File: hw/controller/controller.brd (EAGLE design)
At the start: 46 x 53 mm, 97 parts, among them IC1 STM32G474CEU6, J1 XT30XT30PW_MALE, J2 XT30XT30PW_MALE, Q1 TPH1R204PLSOP_ADVANCE_8, Q2 TPH1R204PLSOP_ADVANCE_8, Q3 TPH1R204PLSOP_ADVANCE_8, Q4 TPH1R204PLSOP_ADVANCE_8, Q5 TPH1R204PLSOP_ADVANCE_8, Q6 TPH1R204PLSOP_ADVANCE_8, U2 DRV8323RS, U3 AS5147, U4 TCAN334G

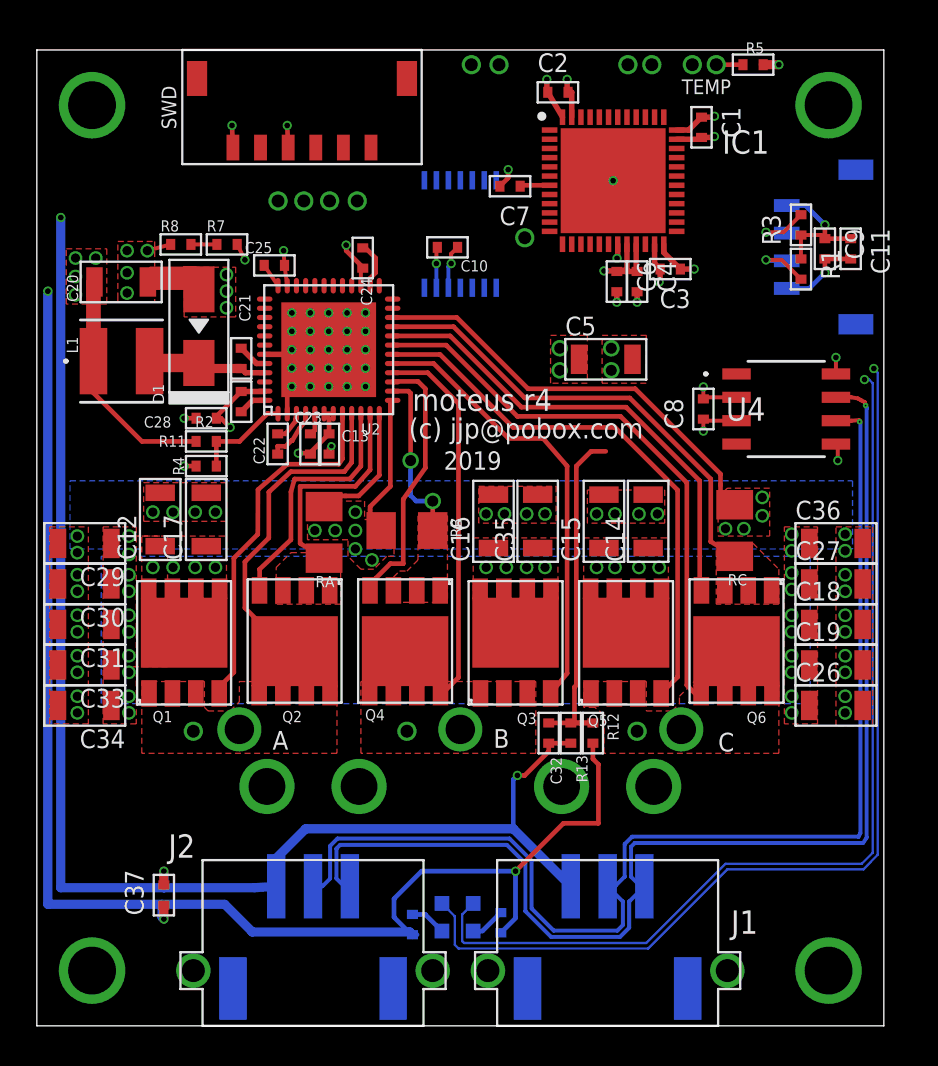
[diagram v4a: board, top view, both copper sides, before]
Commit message: All silks rough placed and all part numbers fixed up
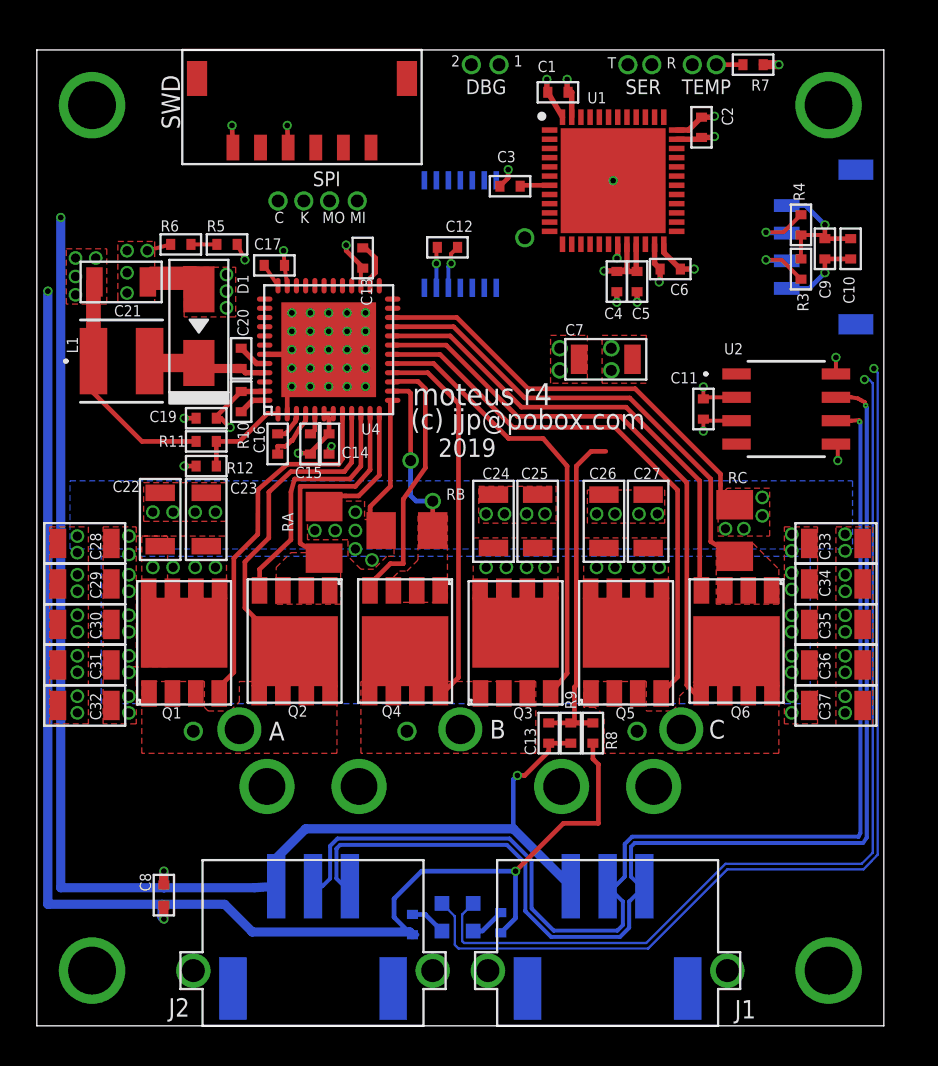
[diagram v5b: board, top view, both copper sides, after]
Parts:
- removed R13: 10k 1%, mfpassives:R0402
- added R10: 100k 1%, mfpassives:R0402
- C1, C10, C11, C13, C2, C3, C8: value 0.1uF 50V -> 0.1uF
- C12, C18, C5: value 10uF -> 0.1uF; device mfpassives:C1206 -> mfpassives:C0402
- C14, C16, C20: value 10uF -> 0.1uF 50V; device mfpassives:C1206 -> mfpassives:C0402
- C15, C17: value 10uF -> 1uF; device mfpassives:C1206 -> mfpassives:C0402
- C19: value 10uF -> 0.47uF 50V; device mfpassives:C1206 -> mfpassives:C0402
- C21, C22, C32, C37, C7: value 0.1uF 50V -> 10uF; device mfpassives:C0402 -> mfpassives:C1206
- C23, C24, C25, C28: value 1.5uF 35V -> 10uF; device mfpassives:C0402 -> mfpassives:C1206
- C4: value 0.1uF 50V -> 1uF
- C6: value 1uF -> 0.1uF
- R1: value 2k -> 220
- R12: value 47k NTC -> 10k 1%
- R2: value 100k 1% -> 220
- R4: value 10k 1% -> 2k
- R5: value 10k 1% -> 100k 1%
- R6, R9: value 220 -> 10k 1%
- R7: value 100k 1% -> 10k 1%
- R8: value 10k 1% -> 47k NTC
- U2: value DRV8323RS -> TCAN334G; device controller:PVQFN-N48 -> controller:SOT23-8
- U4: value TCAN334G -> DRV8323RS; device controller:SOT23-8 -> controller:PVQFN-N48
- moved R1 41.4 mm to (-2.60, -37.5), flipped to the bottom, turned to 90 degrees
- moved C33 41.3 mm to (20.4, -16.8), turned to 0 degrees
- moved C34 41.3 mm to (20.4, -19.0), turned to 0 degrees
- moved C8 39.4 mm to (-16.1, -35.9)
- moved R6 39.0 mm to (-15.2, -0.56), flipped to the top, turned to 0 degrees
- moved C37 37.9 mm to (20.4, -25.6), turned to 0 degrees
- moved C19 36.7 mm to (-13.8, -10.0), turned to 180 degrees
- moved R4 34.9 mm to (18.5, 0.50), turned to 90 degrees
- moved R8 34.7 mm to (7.20, -27.1), turned to 90 degrees
- moved C18 32.5 mm to (-5.30, -1.30), turned to 90 degrees
- moved R2 31.6 mm to (2.20, -37.4), flipped to the bottom
- moved R5 30.2 mm to (-12.7, -0.56)
- moved R7 30.2 mm to (15.9, 9.20)
- moved R12 25.5 mm to (-13.8, -12.6), turned to 180 degrees
- moved C32 25.2 mm to (-20.4, -25.6), turned to 180 degrees
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- renumbered IC1 to U1, U$12 to M2, U$13 to M3, U$14 to M4, U$9 to M1
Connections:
- net +3V3: now also C12.P$1, C18.P$2, C21.P$1, C5.P$1, C7.P$2, R2.P$1, R4.P$1, R8.P$1, U2.3, U4.26; no longer C20.P$1, C24.P$2, C3.P$1, C37.P$1, C5.P$2, R12.P$1, R6.P$1, R9.P$1, U2.26, U4.3
- net CAN_N: now also U2.6; no longer U4.6
- net CAN_P: now also U2.7; no longer U4.7
- net CAN_RX: now also U2.4; no longer U4.4
- net CAN_TX: now also U2.1; no longer U4.1
- net CUR1: now also U4.25; no longer U2.25
- net CUR2: now also U4.24; no longer U2.24
- net CUR3: now also U4.23; no longer U2.23
- net DRV8323_CS: now also U4.32; no longer U2.32
- net DRV8323_MISO: now also U4.29; no longer U2.29
- net DRV8323_MOSI: now also U4.30; no longer U2.30
- net DRV8323_SCLK: now also U4.31; no longer U2.31
- net GHA: now also U4.8; no longer U2.8
- net GHB: now also U4.17; no longer U2.17
- net GHC: now also U4.18; no longer U2.18
- net GLA: now also U4.10; no longer U2.10
- net GLB: now also U4.15; no longer U2.15
- net GLC: now also U4.20; no longer U2.20
- net GND: now also C12.P$2, C13.P$2, C17.P$1, C18.P$1, C21.P$2, C5.P$2, C7.P$1, R6.P$1, R7.P$2, R9.P$2, U2.2, U2.5, U2.8, U4.27, U4.35; no longer C20.P$2, C24.P$1, C25.P$1, C32.P$2, C37.P$2, C5.P$1, C7.P$2, R13.P$2, R5.P$2, R8.P$1, U2.27, U2.35, U4.2, U4.5, U4.8
- net I2C_ABS_SCL: now also R4.P$2; no longer R3.P$2
- net I2C_ABS_SDA: now also R3.P$2; no longer R1.P$2
- net MOTOR1: now also U4.37; no longer U2.37
- net MOTOR2: now also U4.39; no longer U2.39
- net MOTOR3: now also U4.41; no longer U2.41
- net MOTOR_ENABLE: now also U4.33; no longer U2.33
- net MOTOR_FAULT: now also U4.28; no longer U2.28
- net MOTOR_HIZ: now also U4.38, U4.40, U4.42; no longer U2.38, U2.40, U2.42
- net N$10: now also C16.P$2, U4.3; no longer C22.P$2, U2.3
- net N$11: now also C20.P$2, U4.45; no longer C21.P$2, U2.45
- net N$12: now also C20.P$1, U4.44; no longer C21.P$1, U2.44
- net N$13: now also C16.P$1, U4.4; no longer C22.P$1, U2.4
- net N$14: now also C15.P$2, U4.5; no longer C23.P$2, U2.5
- net N$16: now also C17.P$2, U4.36; no longer C25.P$2, U2.36
- net N$17: now also R1.P$2; no longer R6.P$2
- net N$18: now also R2.P$2; no longer R9.P$2
- net N$5: now also R10.P$1, U4.48; no longer R2.P$1, U2.48
- net N$8: now also R12.P$1, U4.1; no longer R4.P$1, U2.1
- net NRST: now also C3.P$1; no longer C7.P$1
- net SHA: now also U4.9; no longer U2.9
- net SHB: now also U4.16; no longer U2.16
- net SHC: now also U4.19; no longer U2.19
- net SNA: now also U4.12; no longer U2.12
- net SNB: now also U4.13; no longer U2.13
- net SNC: now also U4.22; no longer U2.22
- net SPA: now also U4.11; no longer U2.11
- net SPB: now also U4.14; no longer U2.14
- net SPC: now also U4.21; no longer U2.21
- net V+: now also C22.P$1, C24.P$1, C25.P$1, C32.P$1, C37.P$1, R10.P$2, R5.P$2, U4.47, U4.6, U4.7; no longer C12.P$1, C13.P$1, C16.P$1, C17.P$1, C18.P$1, R2.P$2, R7.P$2, U2.47, U2.6, U2.7
- net V-: now also C22.P$2, C23.P$2, C24.P$2, C25.P$2, C32.P$2, C37.P$2, R12.P$2, U4.2, U4.43, U4.P1, U4.P10, U4.P11, U4.P12, U4.P13, U4.P14, U4.P15, U4.P16, U4.P17, U4.P18, U4.P19, U4.P2, U4.P20, U4.P21, U4.P22, U4.P23, U4.P24, U4.P25, U4.P3, U4.P4, U4.P5, U4.P6, U4.P7, U4.P8, U4.P9, U4.PAD; no longer C12.P$2, C13.P$2, C15.P$2, C16.P$2, C17.P$2, C18.P$2, R4.P$2, U2.2, U2.43, U2.P1, U2.P10, U2.P11, U2.P12, U2.P13, U2.P14, U2.P15, U2.P16, U2.P17, U2.P18, U2.P19, U2.P2, U2.P20, U2.P21, U2.P22, U2.P23, U2.P24, U2.P25, U2.P3, U2.P4, U2.P5, U2.P6, U2.P7, U2.P8, U2.P9, U2.PAD
- net VBAT_SENSE: now also R5.P$1, R6.P$2; no longer R7.P$1, R8.P$2
- net VTEMP_FET: now also C13.P$1, R8.P$2, R9.P$1; no longer C32.P$1, R12.P$2, R13.P$1
- net VTEMP_MOT: now also R7.P$1; no longer R5.P$1
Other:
- board text added: "1"
- board text added: "2"
- board text added: "DBG"
- board text added: "K"
- board text added: "MI"
- board text added: "MO"
- board text added: "R"
- board text added: "SER"
- board text added: "SPI"
- board text added: "T"

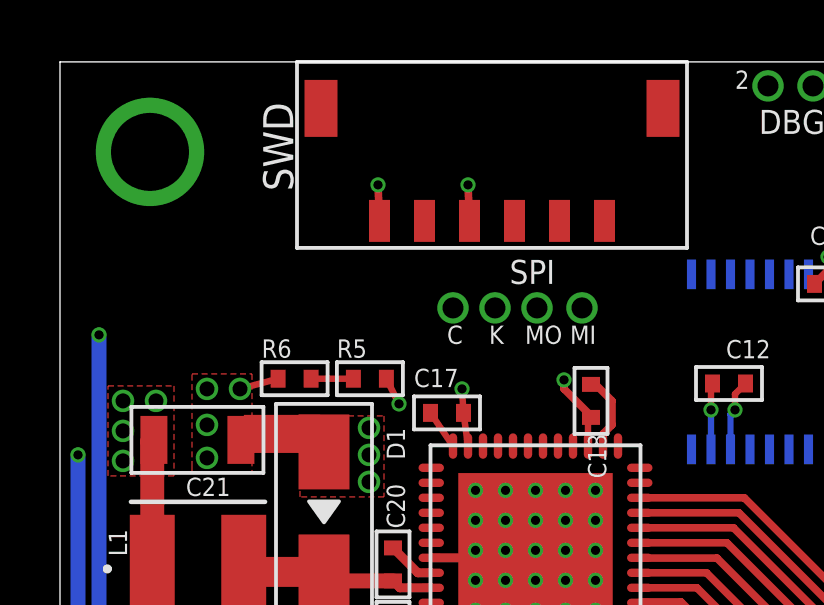
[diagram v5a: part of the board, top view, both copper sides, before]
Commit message: Added some more debugging pads
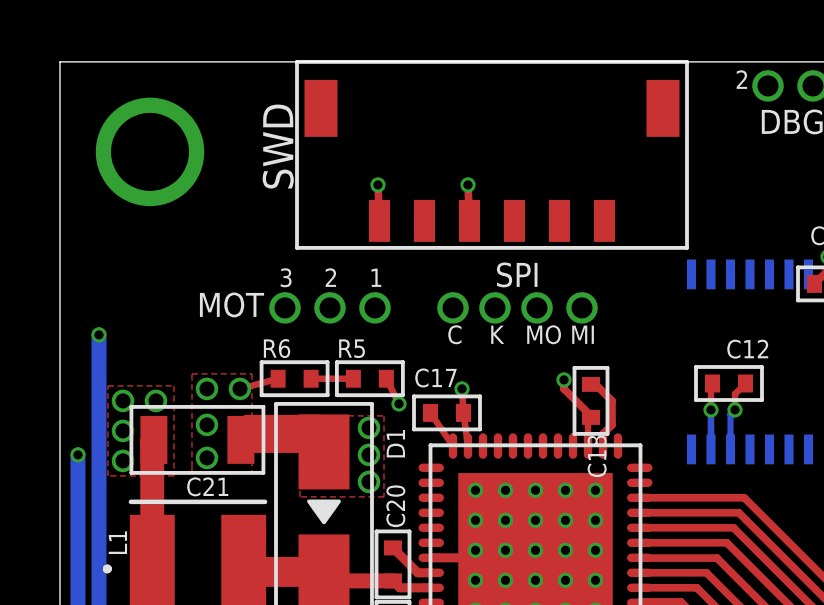
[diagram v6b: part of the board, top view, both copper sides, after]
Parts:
- added MOT1, MOT2, MOT3: PAD24AWG_PAD, controller:24AWG_PAD
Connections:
- net MOTOR1: now also MOT1.P$1
- net MOTOR2: now also MOT2.P$1
- net MOTOR3: now also MOT3.P$1
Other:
- board text added: "3"
- board text added: "MOT"
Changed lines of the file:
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@@
 <layers>
 <layer number="1" name="Top" color="4" fill="1" visible="yes" active="yes"/>
-<layer number="2" name="Route2" color="1" fill="3" visible="no" active="yes"/>
+<layer number="2" name="Route2" color="1" fill="3" visible="yes" active="yes"/>
 <layer number="3" name="Route3" color="4" fill="3" visible="no" active="no"/>
 <layer number="4" name="Route4" color="1" fill="4" visible="no" active="no"/>
@@
 <layer number="13" name="Route13" color="4" fill="5" visible="no" active="no"/>
 <layer number="14" name="Route14" color="1" fill="6" visible="no" active="no"/>
-<layer number="15" name="Route15" color="4" fill="6" visible="no" active="yes"/>
+<layer number="15" name="Route15" color="4" fill="6" visible="yes" active="yes"/>
 <layer number="16" name="Bottom" color="1" fill="1" visible="yes" active="yes"/>
 <layer number="17" name="Pads" color="2" fill="1" visible="yes" active="yes"/>
@@
 <text x="-0.5" y="9.1" size="0.6096" layer="21" font="vector">2</text>
 <text x="2.9" y="9.1" size="0.6096" layer="21" font="vector">1</text>
-<text x="-6.5" y="3.4" size="0.8" layer="21" rot="R180">SPI</text>
+<text x="-8.5" y="2.5" size="0.8" layer="21">SPI</text>
 <text x="-10.1" y="0.6" size="0.6096" layer="21" font="vector">C</text>
 <text x="-8.7" y="0.6" size="0.6096" layer="21" font="vector">K</text>
 <text x="-7.5" y="0.6" size="0.6096" layer="21" font="vector">MO</text>
 <text x="-6" y="0.6" size="0.6096" layer="21" font="vector">MI</text>
+<text x="-12.7" y="2.5" size="0.6096" layer="21" font="vector">1</text>
+<text x="-14.2" y="2.5" size="0.6096" layer="21" font="vector">2</text>
+<text x="-15.7" y="2.5" size="0.6096" layer="21" font="vector">3</text>
+<text x="-16.2" y="2.3" size="0.8" layer="21" rot="R180">MOT</text>
 </plain>
 <attributes>
@@
 <attribute name="POPULATE" value="0" x="-8.5" y="1.8" size="1.778" layer="27" display="off"/>
 </element>
+<element name="MOT1" library="controller" package="24AWG_PAD" value="PAD24AWG_PAD" x="-12.5" y="1.8">
+<attribute name="POPULATE" value="0" x="-12.5" y="1.8" size="0.6096" layer="27" font="vector" display="off"/>
+</element>
+<element name="MOT2" library="controller" package="24AWG_PAD" value="PAD24AWG_PAD" x="-14" y="1.8">
+<attribute name="POPULATE" value="0" x="-14" y="1.8" size="0.6096" layer="27" font="vector" display="off"/>
+</element>
+<element name="MOT3" library="controller" package="24AWG_PAD" value="PAD24AWG_PAD" x="-15.5" y="1.8">
+<attribute name="POPULATE" value="0" x="-15.5" y="1.8" size="0.6096" layer="27" font="vector" display="off"/>
+</element>
 </elements>
 <signals>
@@
 <contactref element="U4" pad="37"/>
 <contactref element="U1" pad="8"/>
+<contactref element="MOT1" pad="P$1"/>
+<wire x1="-10.625" y1="-3.53" x2="-12.5" y2="1.8" width="0" layer="19" extent="1-1"/>
 <wire x1="4.85" y1="2.15" x2="-10.625" y2="-3.53" width="0" layer="19" extent="1-1"/>
 </signal>
@@
 <contactref element="U4" pad="39"/>
 <contactref element="U1" pad="9"/>
+<contactref element="MOT2" pad="P$1"/>
+<wire x1="-14" y1="1.8" x2="-10.625" y2="-4.53" width="0" layer="19" extent="1-1"/>
 <wire x1="4.85" y1="1.65" x2="-10.625" y2="-4.53" width="0" layer="19" extent="1-1"/>
 </signal>
@@
 <contactref element="U4" pad="41"/>
 <contactref element="U1" pad="10"/>
+<contactref element="MOT3" pad="P$1"/>
+<wire x1="-15.5" y1="1.8" x2="-10.625" y2="-5.53" width="0" layer="19" extent="1-1"/>
 <wire x1="4.85" y1="1.15" x2="-10.625" y2="-5.53" width="0" layer="19" extent="1-1"/>
 </signal>

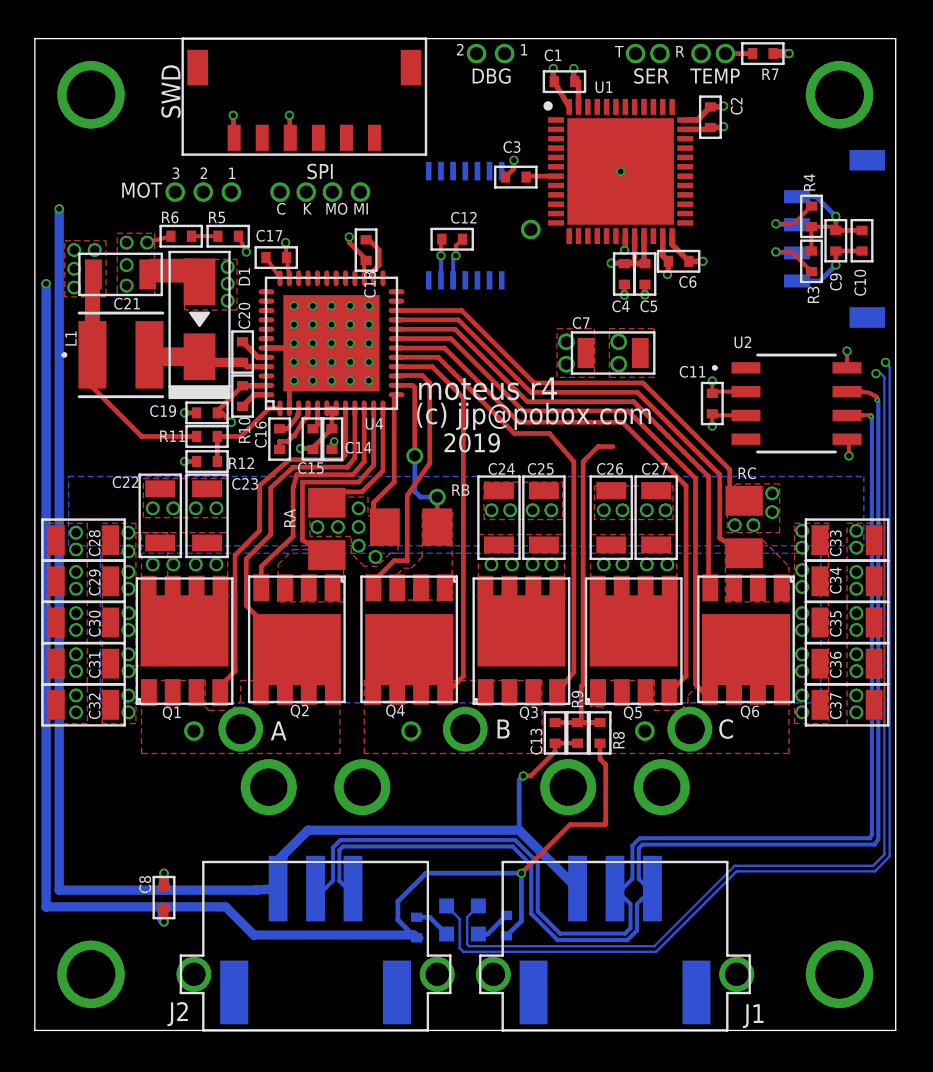
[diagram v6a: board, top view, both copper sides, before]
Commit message: Nearly final version
Still need to verify the footprints of all the JST connectors
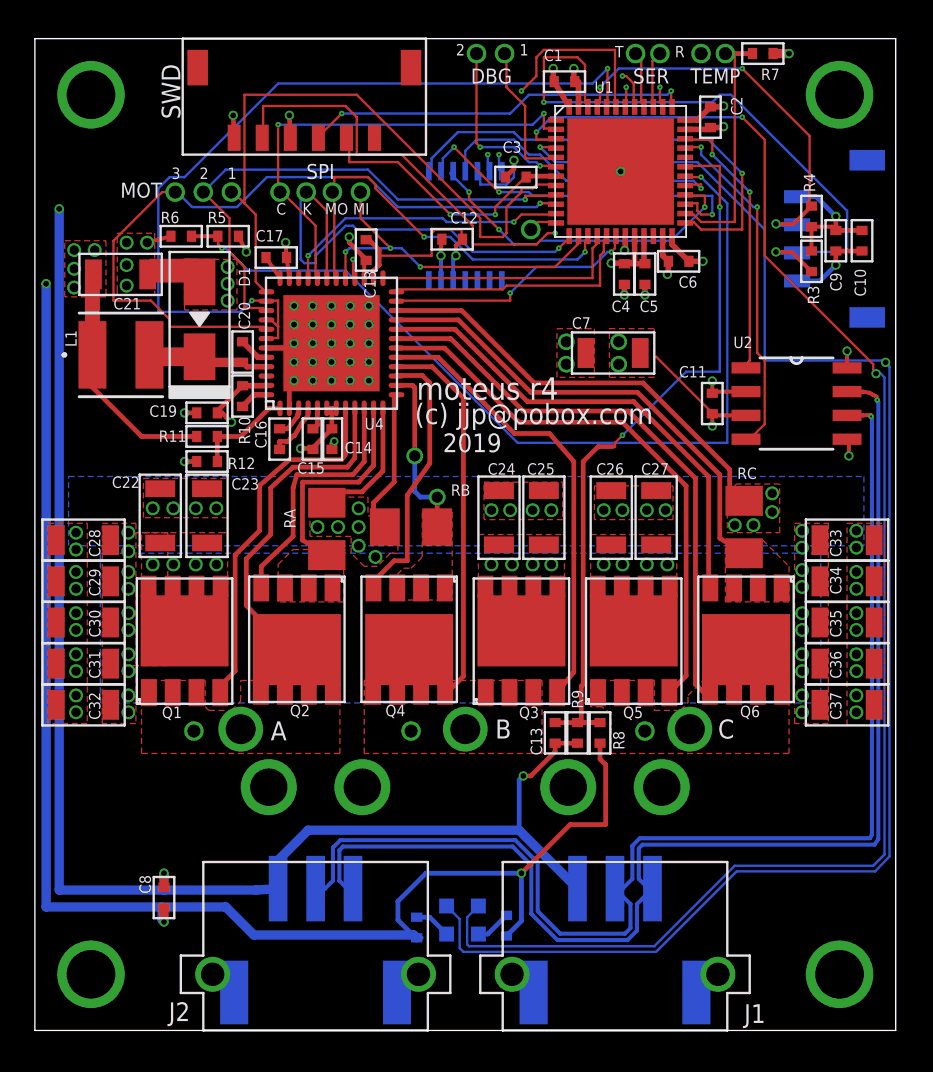
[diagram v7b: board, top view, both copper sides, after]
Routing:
- net VBAT_SENSE: track 1.41 -> 49.1 mm, vias 0 -> 2
- net MOTOR_HIZ: track 0.00 -> 45.4 mm, vias 0 -> 2
- net MOTOR3: track 0.00 -> 38.7 mm, vias 0 -> 1
- net MOTOR1: track 0.00 -> 34.5 mm
- net SWCLK: track 0.00 -> 33.7 mm, vias 0 -> 2
- net I2C_ABS_SDA: track 3.49 -> 34.4 mm, vias 1 -> 2
- net LED2: track 52.8 -> 82.3 mm, vias 1 -> 3
- net MOTOR2: track 0.00 -> 28.6 mm, vias 0 -> 1
- net LED1: track 54.3 -> 82.5 mm, vias 1 -> 2
- net DRV8323_SCLK: track 0.00 -> 25.5 mm, vias 0 -> 1
- net DRV8323_CS: track 0.00 -> 25.2 mm, vias 0 -> 2
- net AS5047_CS: track 0.00 -> 25.1 mm, vias 0 -> 1
- net MOTOR_FAULT: track 0.00 -> 23.4 mm, vias 0 -> 2
- net DRV8323_MOSI: track 0.00 -> 22.1 mm, vias 0 -> 2
- net SWDIO: track 0.00 -> 20.8 mm, vias 0 -> 2
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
